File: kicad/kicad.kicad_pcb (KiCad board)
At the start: 2 copper layers, 41 x 52 mm, 4 parts, among them SW1 SW_Push, U1 nice_nano, U2 GY-BNO08X, U3 SSD1306_OLED_042

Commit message: started working on new pcb
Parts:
- added ?: , , F.Cu at (173.5, 52.5)
- added REF**: MountingHole_2.1mm, MountingHole:MountingHole_2.1mm, F.Cu at (200.5, 52.5)
- added REF**: SolderWire-0.1sqmm_1x01_D0.4mm_OD1mm, Connector_Wire:SolderWire-0.1sqmm_1x01_D0.4mm_OD1mm, F.Cu at (199.5, 86.0)
- added REF**: SolderWire-0.1sqmm_1x01_D0.4mm_OD1mm, Connector_Wire:SolderWire-0.1sqmm_1x01_D0.4mm_OD1mm, F.Cu at (177.5, 86.0)
- added SW2: SW_Push, Button_Switch_SMD:SW_Push_1P1T_NO_CK_KSC6xxG, F.Cu at (187.6, 72.0)
- moved SW1 3.03 mm to (187.4, 79.0)
- moved U2 3.00 mm to (199.6, 90.5)
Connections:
- U1 pad 17: unconnected-(U1-P1.15-Pad17) -> Net-(U1-P1.15)
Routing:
- net (no net): track 0.00 -> 34.7 mm
- net unconnected-(U1-BATIN/P0.04-Pad24): track 0.00 -> 33.9 mm
- net GND: track 74.3 -> 83.2 mm
- net Net-(U1-P1.15): track 0.00 -> 3.91 mm
- net Net-(U1-VCC): track 39.9 -> 43.8 mm
- net Net-(U1-P1.06): track 14.3 -> 17.3 mm
- net Net-(U1-P1.04): track 17.9 -> 20.9 mm
- net Net-(U1-P1.11): track 4.13 -> 3.20 mm
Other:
- board size 41 x 52 mm -> 32 x 56.5 mm

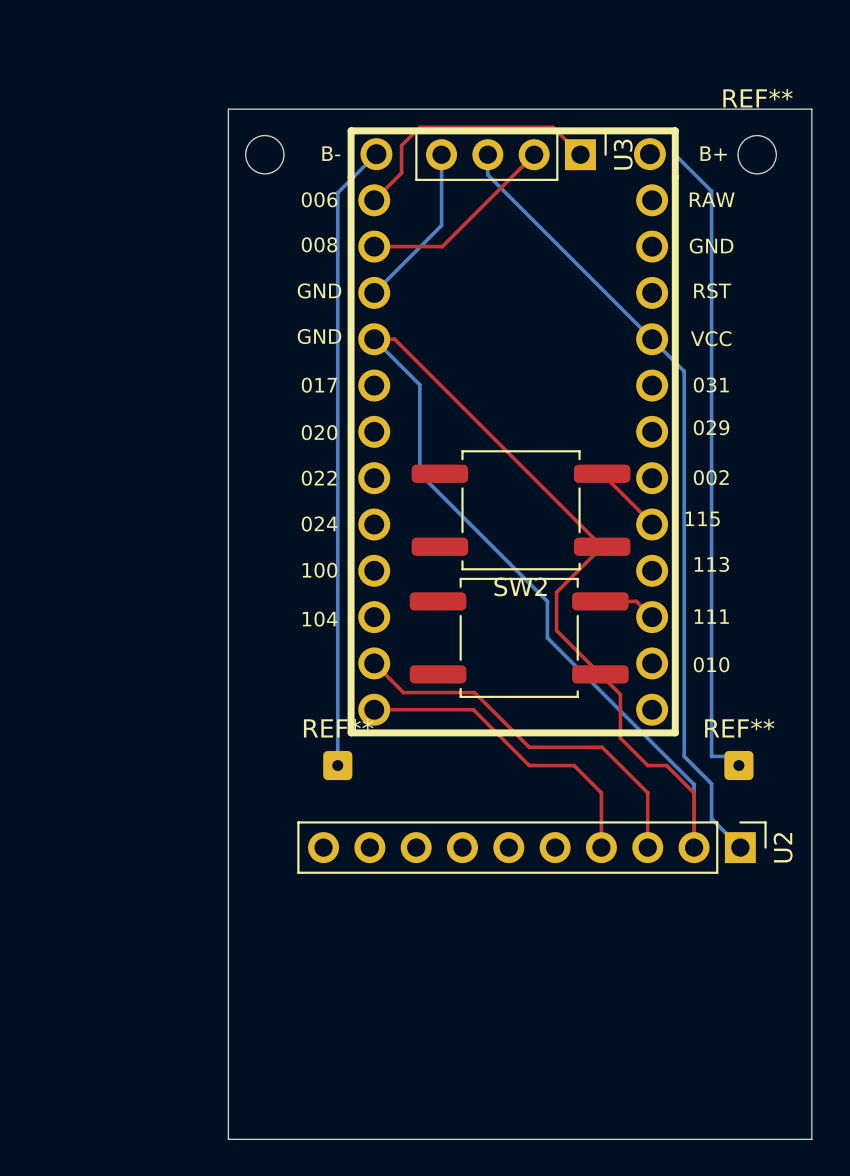
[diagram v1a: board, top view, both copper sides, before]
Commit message: add b+ and b- pins
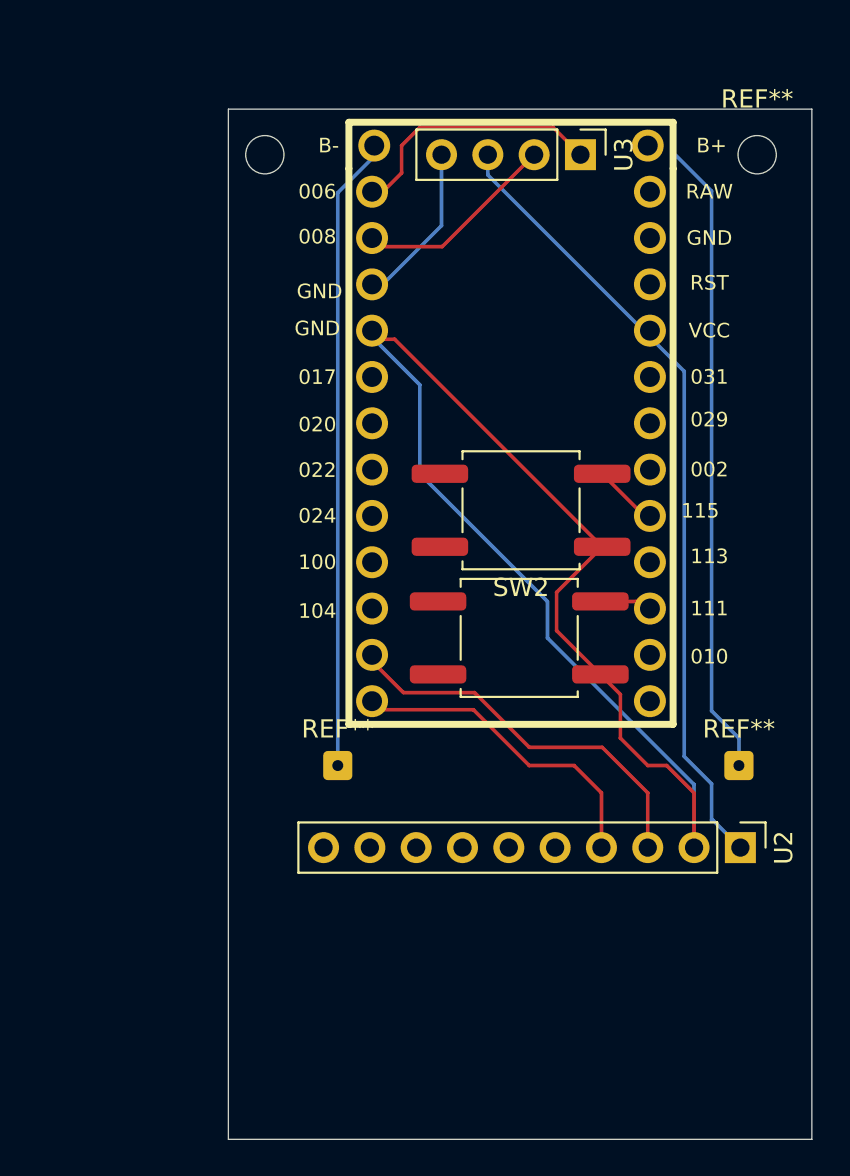
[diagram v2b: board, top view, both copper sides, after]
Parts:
- U1: footprint nice_nano:nice_nano -> nice_nano:nice_nano_with_bat_pins
- moved U1 0.49 mm to (187.0, 68.5)
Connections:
- REF** pad 1: (no net) -> Net-(U1-B+)
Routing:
- net Net-(U1-B+): track 0.00 -> 34.4 mm
- net unconnected-(U1-P0.04-Pad24): track 33.9 -> 0.00 mm

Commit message: fix b+ and b- traces in pcb
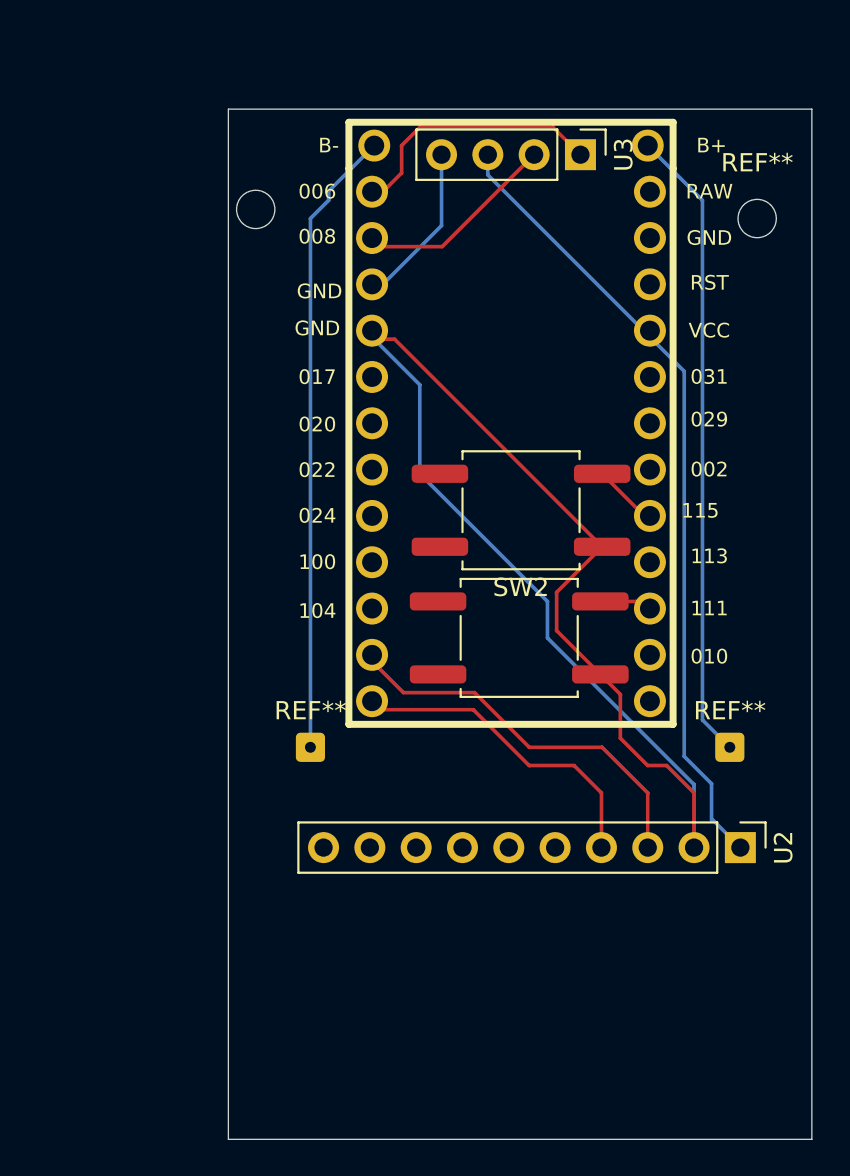
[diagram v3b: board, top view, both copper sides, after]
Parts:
- removed the REF** at (199.5, 86.0)
- removed the REF** at (177.5, 86.0)
- added REF**: SolderWire-0.1sqmm_1x01_D0.4mm_OD1mm, Connector_Wire:SolderWire-0.1sqmm_1x01_D0.4mm_OD1mm, F.Cu at (176.0, 85.0)
- added REF**: SolderWire-0.1sqmm_1x01_D0.4mm_OD1mm, Connector_Wire:SolderWire-0.1sqmm_1x01_D0.4mm_OD1mm, F.Cu at (199.0, 85.0)
- moved REF** 3.50 mm to (200.5, 56.0)
- moved ? 3.04 mm to (173.0, 55.5)
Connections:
- U1 pad 25: Net-(U1-B+) -> unconnected-(U1-B+-Pad25)
- U1 pad 26: Net-(U1-B+) -> unconnected-(U1-B--Pad26)
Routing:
- net (no net): track 34.9 -> 0.00 mm
- net unconnected-(U1-B+-Pad25): track 0.00 -> 34.9 mm
- net unconnected-(U1-B--Pad26): track 0.00 -> 34.4 mm
- net Net-(U1-B+): track 34.4 -> 0.00 mm
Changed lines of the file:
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@@
 	(net 26 "unconnected-(U1-AIN7{slash}P0.31-Pad20)")
 	(net 27 "unconnected-(U1-NFC2{slash}P0.10-Pad14)")
-	(net 28 "Net-(U1-B+)")
-	(net 29 "unconnected-(U1-P0.04-Pad24)")
+	(net 28 "unconnected-(U1-P0.04-Pad24)")
+	(net 29 "unconnected-(U1-B--Pad26)")
+	(net 30 "unconnected-(U1-B+-Pad25)")
 	(footprint "MountingHole:MountingHole_2.1mm"
 		(layer "F.Cu")
-		(at 200.5 52.5)
+		(at 200.5 56)
 		(descr "Mounting Hole 2.1mm, no annular, generated by kicad-footprint-generator mountinghole.py")
 		(tags "mountinghole")
@@
 	(footprint ""
 		(layer "F.Cu")
-		(at 173.5 52.5)
+		(at 173 55.5)
 		(property "Reference" ""
 			(at 0 0 0)
@@
 	(footprint "Connector_Wire:SolderWire-0.1sqmm_1x01_D0.4mm_OD1mm"
 		(layer "F.Cu")
-		(at 199.5 86)
+		(at 176 85)
 		(descr "Soldered wire connection, for a single 0.1 mm² wire, basic insulation, conductor diameter 0.4mm, outer diameter 1mm, size source Multi-Contact FLEXI-E 0.10 (https://www.staubli.com/content/dam/ecs/catalogs-brochures/TM/CAB-Main-11014119-en.pdf#page=9), bend radius 3 times outer diameter, generated with kicad-footprint-generator")
 		(tags "connector wire 0.1sqmm")
@@
 			(at 0 2 0)
 			(layer "F.Fab")
-			(hide yes)
 			(effects
 				(font
@@
 			(remove_unused_layers no)
 			(roundrect_rratio 0.15625)
+			(net 29 "unconnected-(U1-B--Pad26)")
 		)
 		(embedded_fonts no)
@@
 	(footprint "Connector_Wire:SolderWire-0.1sqmm_1x01_D0.4mm_OD1mm"
 		(layer "F.Cu")
-		(at 177.5 86)
+		(at 199 85)
 		(descr "Soldered wire connection, for a single 0.1 mm² wire, basic insulation, conductor diameter 0.4mm, outer diameter 1mm, size source Multi-Contact FLEXI-E 0.10 (https://www.staubli.com/content/dam/ecs/catalogs-brochures/TM/CAB-Main-11014119-en.pdf#page=9), bend radius 3 times outer diameter, generated with kicad-footprint-generator")
 		(tags "connector wire 0.1sqmm")
@@
 			(at 0 2 0)
 			(layer "F.Fab")
-			(hide yes)
 			(effects
 				(font
@@
 		(fp_text user "${REFERENCE}"
 			(at 0 0 0)
-			(layer "F.Fab")
+			(layer "B.Fab")
 			(effects
 				(font
@@
 			)
 		)
-		(pad "1" thru_hole roundrect
+		(pad "2" thru_hole roundrect
 			(at 0 0)
 			(size 1.6 1.6)
@@
 			(remove_unused_layers no)
 			(roundrect_rratio 0.15625)
-			(net 28 "Net-(U1-B+)")
+			(net 30 "unconnected-(U1-B+-Pad25)")
 		)
 		(embedded_fonts no)
@@
 			(layers "*.Cu" "*.SilkS" "*.Mask")
 			(remove_unused_layers no)
-			(net 29 "unconnected-(U1-P0.04-Pad24)")
+			(net 28 "unconnected-(U1-P0.04-Pad24)")
 			(pinfunction "P0.04")
 			(pintype "input")
@@
 			(layers "*.Cu" "*.SilkS" "*.Mask")
 			(remove_unused_layers no)
-			(net 28 "Net-(U1-B+)")
+			(net 30 "unconnected-(U1-B+-Pad25)")
 			(pinfunction "B+")
 			(pintype "power_in")
@@
 			(layers "*.Cu" "*.SilkS" "*.Mask")
 			(remove_unused_layers no)
-			(net 28 "Net-(U1-B+)")
+			(net 29 "unconnected-(U1-B--Pad26)")
 			(pinfunction "B-")
 			(pintype "passive")
@@
 	)
 	(segment
-		(start 198 83)
-		(end 199.5 84.5)
-		(width 0.2)
-		(layer "B.Cu")
-		(net 0)
-	)
-	(segment
-		(start 198 54.5)
-		(end 198 83)
-		(width 0.2)
-		(layer "B.Cu")
-		(net 0)
-	)
-	(segment
-		(start 196 52.5)
-		(end 198 54.5)
-		(width 0.2)
-		(layer "B.Cu")
-		(net 0)
-	)
-	(segment
-		(start 199.5 84.5)
-		(end 199.5 86)
-		(width 0.2)
-		(layer "B.Cu")
-		(net 0)
-	)
-	(segment
 		(start 191.9 77)
 		(end 193.88 77)
@@
 	)
 	(segment
-		(start 177.5 54.59)
-		(end 177.5 86)
+		(start 179.5 52)
+		(end 177 54.5)
 		(width 0.2)
 		(layer "B.Cu")
-		(net 28)
-	)
-	(segment
-		(start 179.62 52.47)
-		(end 177.5 54.59)
+		(net 29)
+	)
+	(segment
+		(start 176 56)
+		(end 176 85)
 		(width 0.2)
 		(layer "B.Cu")
-		(net 28)
+		(net 29)
+	)
+	(segment
+		(start 177 55)
+		(end 176 56)
+		(width 0.2)
+		(layer "B.Cu")
+		(net 29)
+	)
+	(segment
+		(start 177 54.5)
+		(end 177 55)
+		(width 0.2)
+		(layer "B.Cu")
+		(net 29)
+	)
+	(segment
+		(start 197.5 55)
+		(end 194.5 52)
+		(width 0.2)
+		(layer "B.Cu")
+		(net 30)
+	)
+	(segment
+		(start 197.5 83.5)
+		(end 197.5 55)
+		(width 0.2)
+		(layer "B.Cu")
+		(net 30)
+	)
+	(segment
+		(start 197.5 83.5)
+		(end 199 85)
+		(width 0.2)
+		(layer "B.Cu")
+		(net 30)
 	)
 	(embedded_fonts no)

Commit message: kicad cleanup
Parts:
- added REF**: SW_SPDT_Shouhan_MSK12C02, Button_Switch_SMD:SW_SPDT_Shouhan_MSK12C02, F.Cu at (197.5, 49.0)
- moved REF** 2.55 mm to (201.0, 58.5)
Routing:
- net unconnected-(U1-B+-Pad25): track 34.9 -> 0.00 mm
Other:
- board size 32 x 56.5 mm -> 32 x 59 mm

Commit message: add switch to pcb
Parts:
- removed ?: , 
- removed the REF** at (201.0, 58.5)
- removed the REF** at (197.5, 49.0)
- removed the REF** at (176.0, 85.0)
- removed the REF** at (199.0, 85.0)
- added BAT+1: Conn_01x01, Connector_Wire:SolderWire-0.1sqmm_1x01_D0.4mm_OD1mm, B.Cu at (199.5, 85.5)
- added BAT-1: Conn_01x01, Connector_Wire:SolderWire-0.1sqmm_1x01_D0.4mm_OD1mm, B.Cu at (177.0, 86.5)
- added REF**: MountingHole_2mm, MountingHole:MountingHole_2mm, F.Cu at (176.5, 50.0)
- added REF**: MountingHole_2mm, MountingHole:MountingHole_2mm, F.Cu at (199.5, 55.0)
- added SW_POWER1: SW_SPDT, Button_Switch_SMD:SW_SPDT_Shouhan_MSK12C02, B.Cu at (195.5, 49.0)
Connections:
- U1 pad 25: unconnected-(U1-B+-Pad25) -> Net-(SW_POWER1-B)
- U1 pad 26: unconnected-(U1-B--Pad26) -> Net-(BAT-1-Pin_1)
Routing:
- net Net-(BAT-1-Pin_1): track 0.00 -> 37.5 mm
- net Net-(BAT+1-Pin_1): track 0.00 -> 35.5 mm
- net unconnected-(U1-B--Pad26): track 34.4 -> 0.00 mm
- net Net-(SW_POWER1-B): track 0.00 -> 2.18 mm
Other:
- board size 32 x 59 mm -> 27 x 59 mm

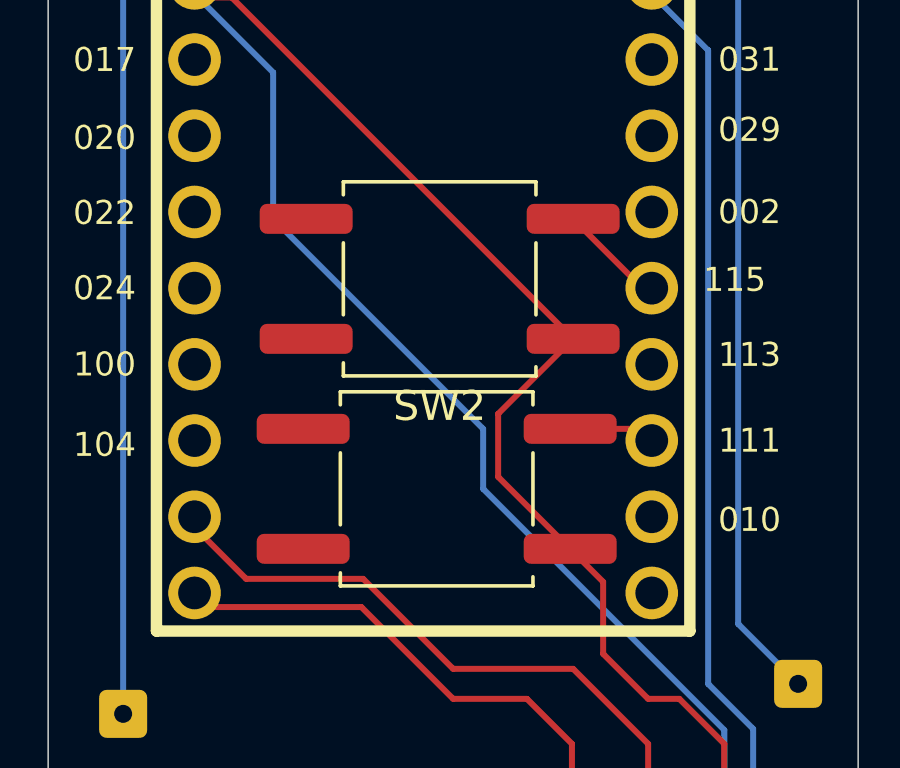
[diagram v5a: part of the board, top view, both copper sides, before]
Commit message: move 2nd button to 113
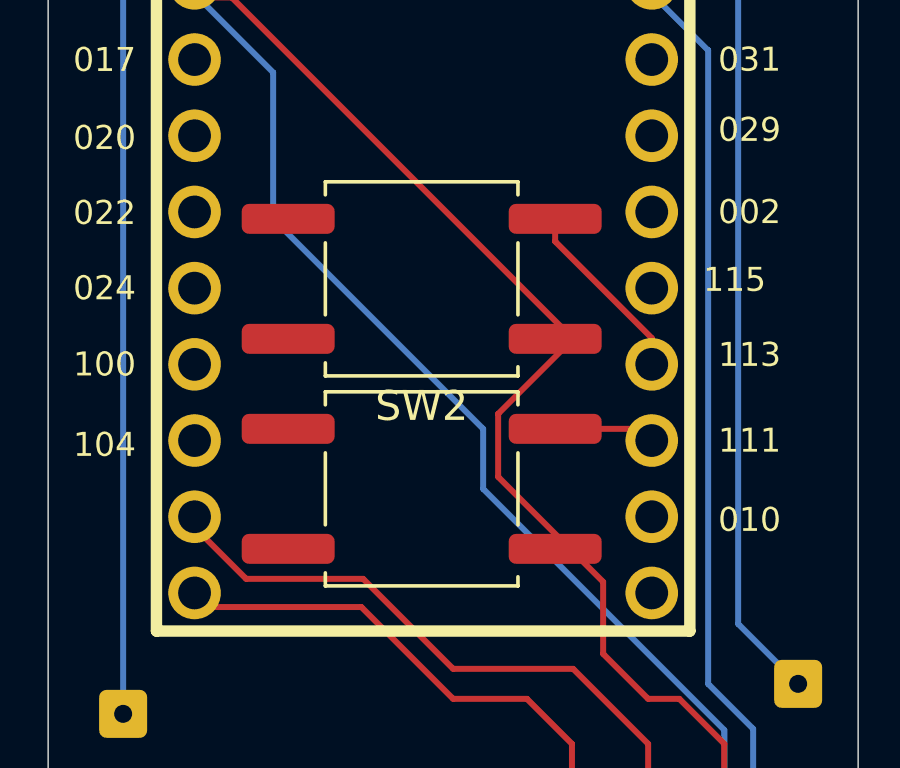
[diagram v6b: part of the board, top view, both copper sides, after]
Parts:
- moved SW2 0.60 mm to (186.9, 72.0)
- moved SW1 0.50 mm to (186.9, 79.0)
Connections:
- SW2 pad 1: Net-(U1-P1.15) -> Net-(U1-P1.13)
- U1 pad 16: unconnected-(U1-P1.13-Pad16) -> Net-(U1-P1.13)
- U1 pad 17: Net-(U1-P1.15) -> unconnected-(U1-P1.15-Pad17)
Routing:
- net Net-(U1-P1.13): track 0.00 -> 6.18 mm
- net Net-(U1-P1.15): track 3.91 -> 0.00 mm
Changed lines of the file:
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@@
 	(net 15 "unconnected-(U1-P0.11-Pad10)")
 	(net 16 "unconnected-(U1-P0.17-Pad5)")
-	(net 17 "unconnected-(U1-P1.13-Pad16)")
-	(net 18 "Net-(U1-P1.15)")
+	(net 17 "Net-(U1-P1.13)")
+	(net 18 "unconnected-(U1-P1.15-Pad17)")
 	(net 19 "unconnected-(U1-P1.00-Pad9)")
 	(net 20 "unconnected-(U1-P0.20-Pad6)")
@@
 	(footprint "Button_Switch_SMD:SW_Push_1P1T_NO_CK_KSC6xxG"
 		(layer "F.Cu")
-		(at 187.55 72)
+		(at 186.95 72)
 		(descr "Tactile switch, 6.2x6.25 mm, H7.7 mm, gullwing leads, https://www.ckswitches.com/media/1972/ksc6.pdf")
 		(tags "CK C&K SPST")
@@
 			(layers "F.Cu" "F.Mask" "F.Paste")
 			(roundrect_rratio 0.25)
-			(net 18 "Net-(U1-P1.15)")
+			(net 17 "Net-(U1-P1.13)")
 			(pinfunction "1")
 			(pintype "passive")
@@
 			(layers "F.Cu" "F.Mask" "F.Paste")
 			(roundrect_rratio 0.25)
-			(net 18 "Net-(U1-P1.15)")
+			(net 17 "Net-(U1-P1.13)")
 			(pinfunction "1")
 			(pintype "passive")
@@
 	(footprint "Button_Switch_SMD:SW_Push_1P1T_NO_CK_KSC6xxG"
 		(layer "F.Cu")
-		(at 187.45 79)
+		(at 186.95 79)
 		(descr "Tactile switch, 6.2x6.25 mm, H7.7 mm, gullwing leads, https://www.ckswitches.com/media/1972/ksc6.pdf")
 		(tags "CK C&K SPST")
@@
 			(layers "*.Cu" "*.SilkS" "*.Mask")
 			(remove_unused_layers no)
-			(net 17 "unconnected-(U1-P1.13-Pad16)")
+			(net 17 "Net-(U1-P1.13)")
 			(pinfunction "P1.13")
 			(pintype "input")
@@
 			(layers "*.Cu" "*.SilkS" "*.Mask")
 			(remove_unused_layers no)
-			(net 18 "Net-(U1-P1.15)")
+			(net 18 "unconnected-(U1-P1.15-Pad17)")
 			(pinfunction "P1.15")
 			(pintype "input")
@@
 	)
 	(segment
-		(start 192 70)
-		(end 194.74 72.74)
-		(width 0.2)
-		(layer "F.Cu")
-		(net 18)
-	)
-	(segment
+		(start 194.62 73.97354)
+		(end 191.4 70.75354)
+		(width 0.2)
+		(layer "F.Cu")
+		(net 17)
+	)
+	(segment
+		(start 191.4 70.75354)
+		(end 191.4 70)
+		(width 0.2)
+		(layer "F.Cu")
+		(net 17)
+	)
+	(segment
+		(start 194.62 74.85)
+		(end 194.62 73.97354)
+		(width 0.2)
+		(layer "F.Cu")
+		(net 17)
+	)
+	(segment
